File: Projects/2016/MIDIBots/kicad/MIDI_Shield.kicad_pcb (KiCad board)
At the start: 2 copper layers, 92.7 x 82.5 mm, 71 parts, among them IC1 PC900V, K1 SRVO1, K2 SRVO2, K3 SRVO3, P10 A3, P11 A4, P12 AUX_12V, P13 AUX_12V, P14 AUX_5V, P15 AUX_5V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

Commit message: Removed test PCB outline/edge cuts
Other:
- board outline removed
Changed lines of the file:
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@@
     (area 50.749999 68.529999 143.560001 151.180001)
     (thickness 1.6)
-    (drawings 19)
+    (drawings 9)
     (tracks 262)
     (zones 0)
@@
     (effects (font (size 1.5 1.5) (thickness 0.3)))
   )
-  (gr_line (start 143.51 110.49) (end 143.51 144.78) (angle 90) (layer Edge.Cuts) (width 0.1))
-  (gr_line (start 143.51 81.28) (end 143.51 110.49) (angle 90) (layer Edge.Cuts) (width 0.1))
-  (gr_line (start 130.81 68.58) (end 143.51 81.28) (angle 90) (layer Edge.Cuts) (width 0.1))
-  (gr_line (start 71.12 68.58) (end 130.81 68.58) (angle 90) (layer Edge.Cuts) (width 0.1))
-  (gr_line (start 50.8 88.9) (end 71.12 68.58) (angle 90) (layer Edge.Cuts) (width 0.1))
-  (gr_line (start 50.8 143.51) (end 50.8 88.9) (angle 90) (layer Edge.Cuts) (width 0.1))
-  (gr_line (start 58.42 151.13) (end 50.8 143.51) (angle 90) (layer Edge.Cuts) (width 0.1))
-  (gr_line (start 59.69 151.13) (end 58.42 151.13) (angle 90) (layer Edge.Cuts) (width 0.1))
-  (gr_line (start 137.16 151.13) (end 59.69 151.13) (angle 90) (layer Edge.Cuts) (width 0.1))
-  (gr_line (start 143.51 144.78) (end 137.16 151.13) (angle 90) (layer Edge.Cuts) (width 0.1))
   (target plus (at 50 60.01) (size 5) (width 0.1) (layer Edge.Cuts))
   (target plus (at 50.01 159.97) (size 5) (width 0.1) (layer Edge.Cuts))
@@
   (segment (start 103.886 126.492) (end 103.886 139.7) (width 0.5) (layer F.Cu) (net 5))
   (segment (start 101.854 124.46) (end 103.886 126.492) (width 0.5) (layer F.Cu) (net 5))
-  (segment (start 73.66 114.3) (end 75.692 114.3) (width 0.5) (layer F.Cu) (net 6) (status 400000))
-  (segment (start 86.614 127) (end 88.9 129.286) (width 0.5) (layer F.Cu) (net 6) (status 800000))
+  (segment (start 73.66 114.3) (end 75.692 114.3) (width 0.5) (layer F.Cu) (net 6))
+  (segment (start 86.614 127) (end 88.9 129.286) (width 0.5) (layer F.Cu) (net 6))
   (segment (start 82.296 127) (end 86.614 127) (width 0.5) (layer F.Cu) (net 6))
   (segment (start 76.708 121.412) (end 82.296 127) (width 0.5) (layer F.Cu) (net 6))
@@
   (segment (start 110.49 112.014) (end 110.49 110.998) (width 0.5) (layer F.Cu) (net 21))
   (segment (start 100.076 127) (end 100.076 129.54) (width 0.5) (layer F.Cu) (net 22))
-  (segment (start 78.74 127) (end 89.154 127) (width 1.25) (layer B.Cu) (net 23) (status 400000))
-  (segment (start 95.758 120.396) (end 95.758 114.3) (width 1.25) (layer B.Cu) (net 23) (status 800000))
+  (segment (start 78.74 127) (end 89.154 127) (width 1.25) (layer B.Cu) (net 23))
+  (segment (start 95.758 120.396) (end 95.758 114.3) (width 1.25) (layer B.Cu) (net 23))
   (segment (start 89.154 127) (end 95.758 120.396) (width 1.25) (layer B.Cu) (net 23))
-  (segment (start 73.66 119.38) (end 74.422 119.38) (width 1.25) (layer B.Cu) (net 23) (status C00000))
-  (segment (start 74.422 119.38) (end 78.74 123.698) (width 1.25) (layer B.Cu) (net 23) (status 400000))
-  (segment (start 78.74 123.698) (end 78.74 127) (width 1.25) (layer B.Cu) (net 23) (status 800000))
+  (segment (start 73.66 119.38) (end 74.422 119.38) (width 1.25) (layer B.Cu) (net 23))
+  (segment (start 74.422 119.38) (end 78.74 123.698) (width 1.25) (layer B.Cu) (net 23))
+  (segment (start 78.74 123.698) (end 78.74 127) (width 1.25) (layer B.Cu) (net 23))
   (segment (start 91.948 115.57) (end 91.948 117.094) (width 1.25) (layer F.Cu) (net 23))
   (segment (start 90.932 118.11) (end 88.9 118.11) (width 1.25) (layer F.Cu) (net 23))
@@
   (segment (start 110.71098 79.121) (end 111.125 79.53502) (width 1.75) (layer F.Cu) (net 32))
   (segment (start 111.125 79.53502) (end 111.125 84.53374) (width 1.75) (layer F.Cu) (net 32))
-  (segment (start 78.486 113.03) (end 80.518 113.03) (width 0.75) (layer F.Cu) (net 33) (status 400000))
-  (segment (start 80.518 113.03) (end 81.788 114.3) (width 0.75) (layer F.Cu) (net 33) (status 800000))
+  (segment (start 78.486 113.03) (end 80.518 113.03) (width 0.75) (layer F.Cu) (net 33))
+  (segment (start 80.518 113.03) (end 81.788 114.3) (width 0.75) (layer F.Cu) (net 33))
   (segment (start 81.788 114.3) (end 81.788 115.824) (width 0.75) (layer F.Cu) (net 33))
   (segment (start 81.28 116.332) (end 81.28 118.11) (width 0.75) (layer F.Cu) (net 33))
   (segment (start 81.788 115.824) (end 81.28 116.332) (width 0.75) (layer F.Cu) (net 33))
-  (segment (start 78.486 120.65) (end 81.28 120.65) (width 0.75) (layer F.Cu) (net 34) (status C00000))
+  (segment (start 78.486 120.65) (end 81.28 120.65) (width 0.75) (layer F.Cu) (net 34))
   (segment (start 76.708 109.22) (end 82.55 109.22) (width 0.75) (layer F.Cu) (net 34))
   (segment (start 83.82 120.65) (end 81.28 120.65) (width 0.75) (layer F.Cu) (net 34))

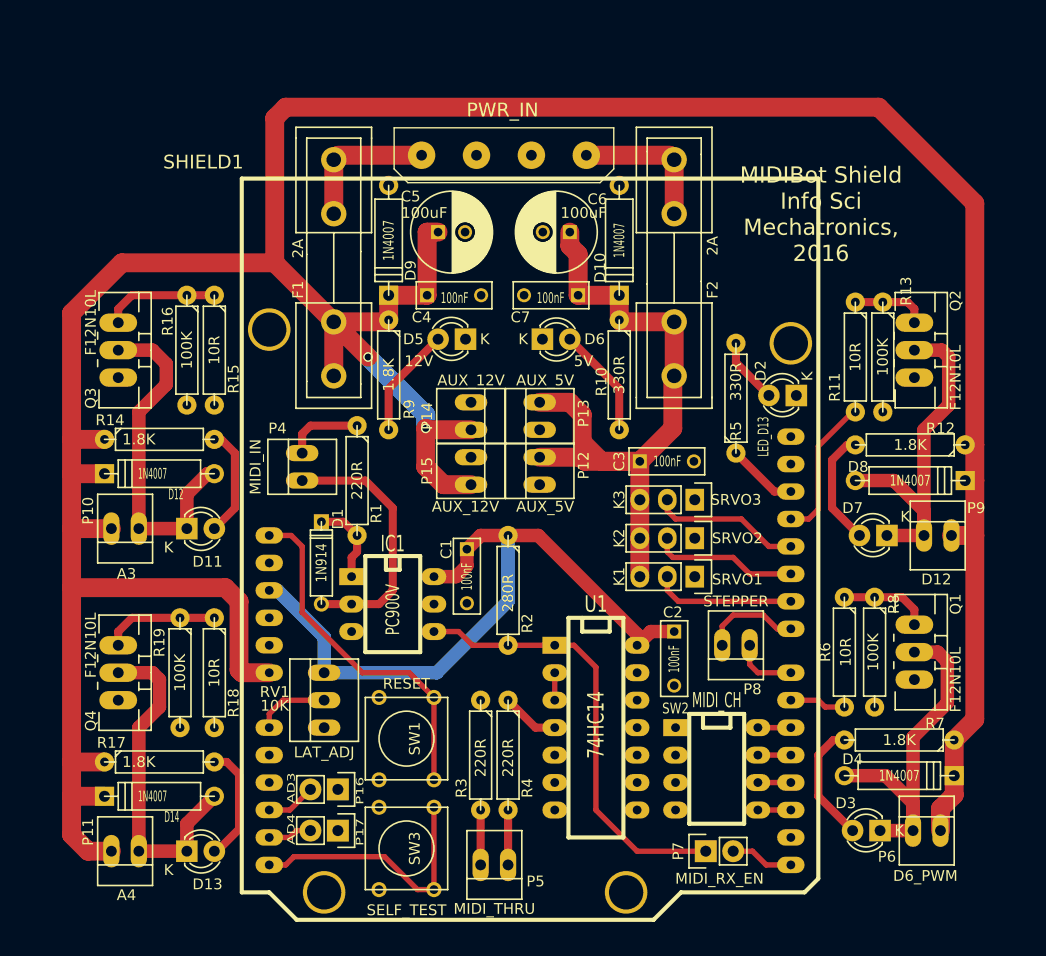
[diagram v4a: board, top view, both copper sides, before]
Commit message: Added missing tracks for MOSFET outputs 3 and 4
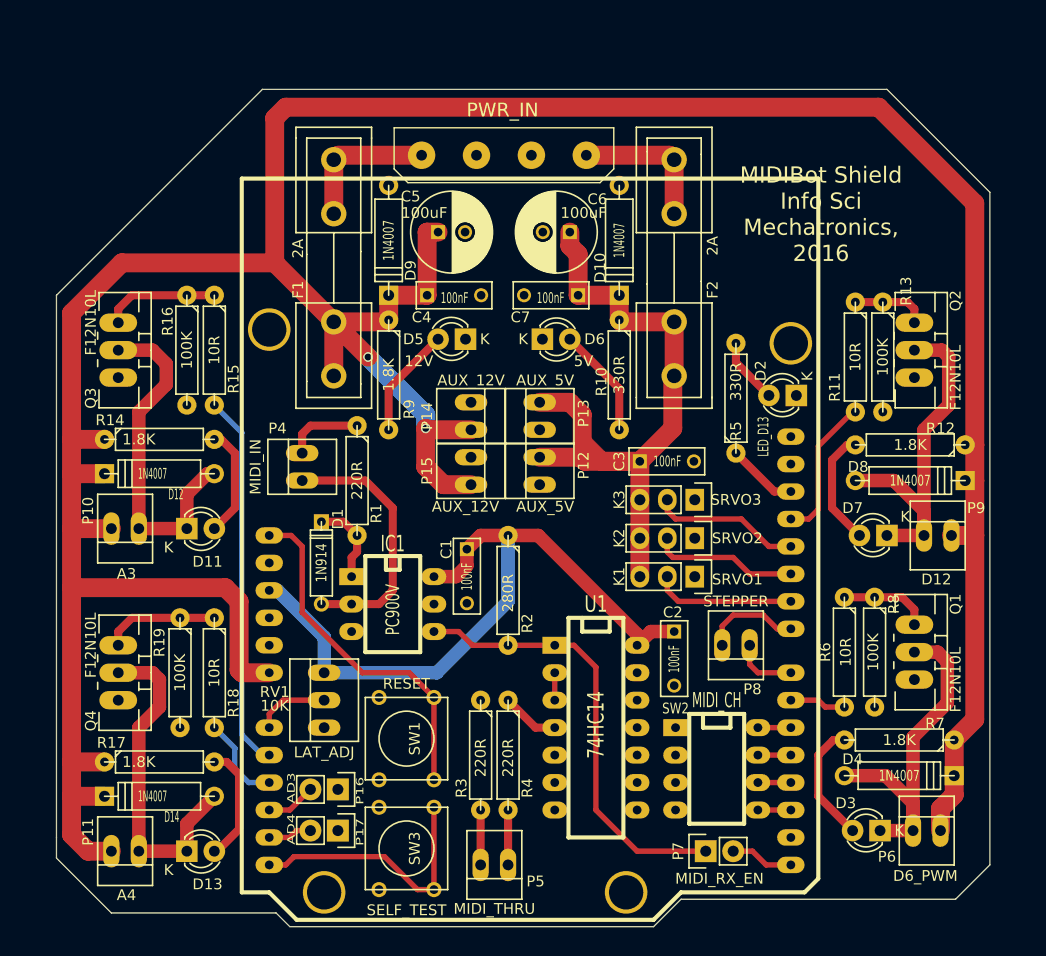
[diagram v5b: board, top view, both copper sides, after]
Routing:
- net /MOSFET_3: track 0.00 -> 34.9 mm
- net /MOSFET_4: track 0.00 -> 8.30 mm
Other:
- board outline added: 86.4 x 77.5 mm
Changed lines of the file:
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@@
   (general
     (links 151)
-    (no_connects 51)
+    (no_connects 49)
     (area 50.749999 68.529999 143.560001 151.180001)
     (thickness 1.6)
-    (drawings 9)
-    (tracks 262)
+    (drawings 22)
+    (tracks 270)
     (zones 0)
     (modules 71)
@@
   (module arduino_shields:ARDUINO_SHIELD locked (layer F.Cu)
     (at 71.12 81.28 270)
-    (fp_text reference SHIELD1 (at -1.524 3.556 360) (layer F.SilkS)
+    (fp_text reference SHIELD1 (at 5.715 5.08 360) (layer F.SilkS) hide
       (effects (font (thickness 0.3048)))
     )
-    (fp_text value ARDUINO_SHIELD (at 4.572 7.874 360) (layer F.SilkS) hide
+    (fp_text value ARDUINO_SHIELD (at -6.35 -50.165 360) (layer F.SilkS) hide
       (effects (font (thickness 0.3048)))
     )
@@
     )
   )
+  (gr_line (start 53.975 144.145) (end 53.975 142.24) (angle 90) (layer Edge.Cuts) (width 0.1))
+  (gr_line (start 59.055 149.225) (end 53.975 144.145) (angle 90) (layer Edge.Cuts) (width 0.1))
+  (gr_line (start 74.295 149.225) (end 59.055 149.225) (angle 90) (layer Edge.Cuts) (width 0.1))
+  (gr_line (start 75.565 150.495) (end 74.295 149.225) (angle 90) (layer Edge.Cuts) (width 0.1))
+  (gr_line (start 109.22 150.495) (end 75.565 150.495) (angle 90) (layer Edge.Cuts) (width 0.1))
+  (gr_line (start 111.76 147.955) (end 109.22 150.495) (angle 90) (layer Edge.Cuts) (width 0.1))
+  (gr_line (start 137.16 147.955) (end 111.76 147.955) (angle 90) (layer Edge.Cuts) (width 0.1))
+  (gr_line (start 140.335 144.78) (end 137.16 147.955) (angle 90) (layer Edge.Cuts) (width 0.1))
+  (gr_line (start 140.335 82.55) (end 140.335 144.78) (angle 90) (layer Edge.Cuts) (width 0.1))
+  (gr_line (start 130.81 73.025) (end 140.335 82.55) (angle 90) (layer Edge.Cuts) (width 0.1))
+  (gr_line (start 73.025 73.025) (end 130.81 73.025) (angle 90) (layer Edge.Cuts) (width 0.1))
+  (gr_line (start 53.975 92.075) (end 73.025 73.025) (angle 90) (layer Edge.Cuts) (width 0.1))
+  (gr_line (start 53.975 142.24) (end 53.975 92.075) (angle 90) (layer Edge.Cuts) (width 0.1))
   (gr_text "MIDIBot Shield\nInfo Sci\nMechatronics,\n2016" (at 124.714 84.582) (layer F.SilkS)
     (effects (font (size 1.5 1.5) (thickness 0.3)))
@@
   (segment (start 123.571 112.776) (end 124.46 111.887) (width 0.5) (layer F.Cu) (net 45))
   (segment (start 127.635 102.87) (end 127.889 102.87) (width 0.5) (layer F.Cu) (net 45))
+  (segment (start 73.66 134.62) (end 73.025 134.62) (width 0.5) (layer B.Cu) (net 46) (status C00000))
+  (segment (start 73.025 134.62) (end 71.12 132.715) (width 0.5) (layer B.Cu) (net 46) (status 400000))
+  (segment (start 71.12 132.715) (end 71.12 104.775) (width 0.5) (layer B.Cu) (net 46))
+  (segment (start 71.12 104.775) (end 68.58 102.235) (width 0.5) (layer B.Cu) (net 46) (status 800000))
+  (segment (start 73.66 137.16) (end 71.755 137.16) (width 0.5) (layer B.Cu) (net 47) (status 400000))
+  (segment (start 70.485 133.985) (end 68.58 132.08) (width 0.5) (layer B.Cu) (net 47) (status 800000))
+  (segment (start 70.485 135.89) (end 70.485 133.985) (width 0.5) (layer B.Cu) (net 47))
+  (segment (start 71.755 137.16) (end 70.485 135.89) (width 0.5) (layer B.Cu) (net 47))
   (segment (start 73.66 139.7) (end 75.565 139.7) (width 0.5) (layer F.Cu) (net 48))
   (segment (start 75.565 139.7) (end 77.47 137.795) (width 0.5) (layer F.Cu) (net 48))

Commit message: Added filled ground plane on back copper layer
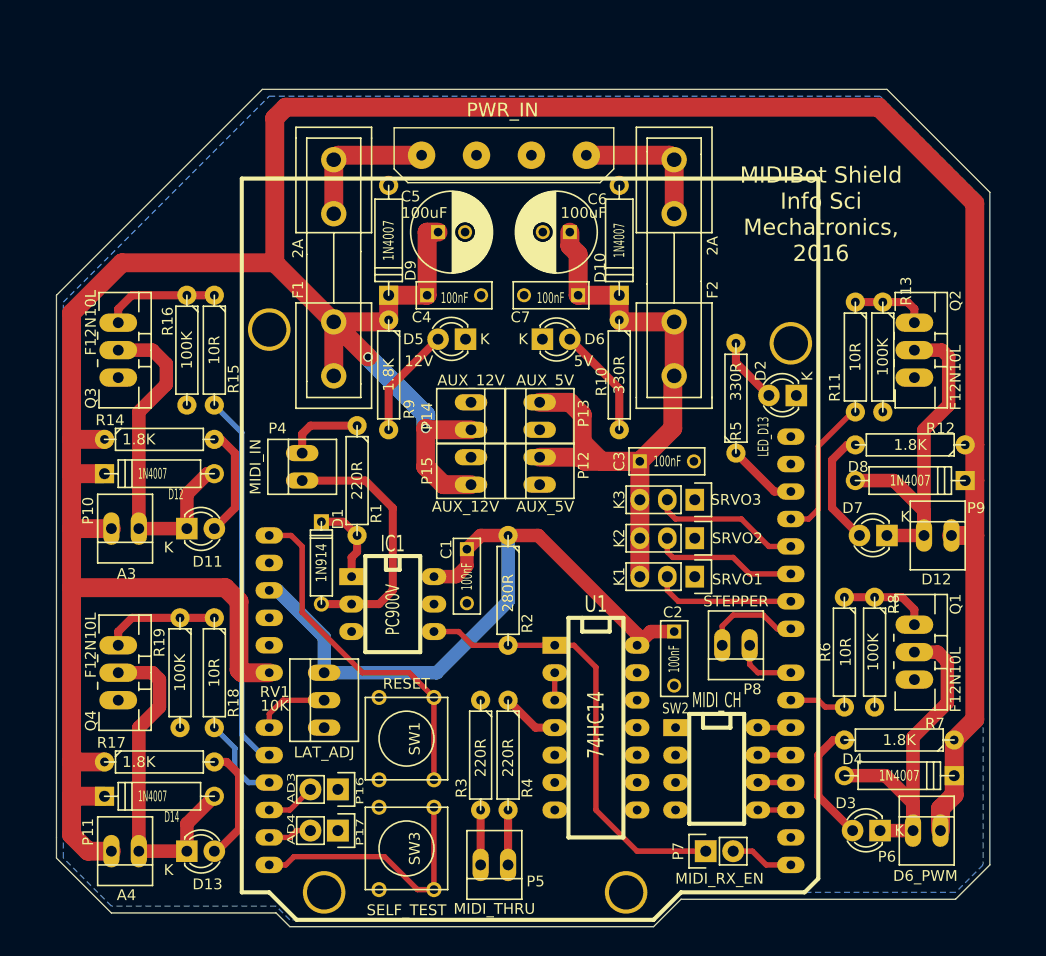
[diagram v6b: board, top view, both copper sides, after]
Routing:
- added copper zone on B.Cu, net GND
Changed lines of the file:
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@@
   (general
     (links 151)
-    (no_connects 49)
+    (no_connects 1)
     (area 50.749999 68.529999 143.560001 151.180001)
     (thickness 1.6)
@@
     (38 B.Mask user)
     (39 F.Mask user)
-    (40 Dwgs.User user hide)
+    (40 Dwgs.User user)
     (41 Cmts.User user)
     (42 Eco1.User user)
@@
   (segment (start 76.2 141.605) (end 77.47 141.605) (width 0.5) (layer F.Cu) (net 49))
   (segment (start 75.565 142.24) (end 76.2 141.605) (width 0.5) (layer F.Cu) (net 49))
+  (zone (net 7) (net_name GND) (layer B.Cu) (hatch edge 0.508)
+    (connect_pads (clearance 0.508))
+    (min_thickness 0.254)
+    (fill yes (arc_segments 16) (thermal_gap 0.508) (thermal_bridge_width 0.508))
+    (polygon
+      (pts
+        (xy 73.66 73.66) (xy 130.175 73.66) (xy 139.7 83.185) (xy 139.7 144.78) (xy 137.16 147.32)
+        (xy 111.76 147.32) (xy 109.22 149.86) (xy 75.565 149.86) (xy 74.295 148.59) (xy 59.055 148.59)
+        (xy 54.61 144.145) (xy 54.61 92.71)
+      )
+    )
+  )
 )
